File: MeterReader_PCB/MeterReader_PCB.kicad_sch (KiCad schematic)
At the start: 10 parts, among them J1 USB_C_Receptacle_USB2.0, J2 SWD_TagConnect, Q2 AO3401A, SW1 SW_DIP_x04, SW2 SW_Push

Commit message: move active components onto sensor PCB, finish layout of sensor PCB
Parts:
- removed SW1: SW_DIP_x04, symbol Switch:SW_DIP_x04
- added BT2, BT3, BT4: 3.7V LiIon, Battery:BatteryHolder_Keystone_1042_1x18650, symbol Device:Battery_Cell
- added C3: 1u, Capacitor_SMD:C_0603_1608Metric, symbol Device:C
- added C4: 100n, Capacitor_SMD:C_0603_1608Metric, symbol Device:C
- added D1, D2, D3, D4, D5, D6, D7, D8: SS34, Diode_SMD:D_SMA, symbol Device:D_Schottky
- added D10: LED, LED_SMD:LED_0603_1608Metric, symbol Device:LED
- added J6, J7: Conn_01x02, Connector_JST:JST_PH_S2B-PH-K_1x02_P2.00mm_Horizontal, symbol Connector_Generic:Conn_01x02
- added J8: USB_C_Receptacle_USB2.0, Connector_USB:USB_C_Receptacle_HRO_TYPE-C-31-M-12, symbol Connector:USB_C_Receptacle_USB2.0
- added LOGO1: Logo_Open_Hardware_Small, Symbol:OSHW-Symbol_6.7x6mm_SilkScreen, symbol Graphic:Logo_Open_Hardware_Small
- added Q3: FS8205A, Package_SO:TSSOP-8_4.4x3mm_P0.65mm, symbol LeoDJ:FS8205A
- added R10: 1k, Capacitor_SMD:C_0603_1608Metric, symbol Device:R
- added R11, R12, R7: 5k1, Resistor_SMD:R_0603_1608Metric, symbol Device:R
- added R8: 2k2, Resistor_SMD:R_0603_1608Metric, symbol Device:R
- added R9: 100, Capacitor_SMD:C_0603_1608Metric, symbol Device:R
- added TP1, TP2: TestPoint, TestPoint:TestPoint_Pad_1.5x1.5mm, symbol Connector:TestPoint
- added U3: LTC4054ES5-4.2, Package_TO_SOT_SMD:TSOT-23-5, symbol Battery_Management:LTC4054ES5-4.2
- added U4: DW01A, Package_TO_SOT_SMD:SOT-23-6, symbol LeoDJ:DW01A
- BT1: footprint (none) -> Battery:BatteryHolder_Keystone_1042_1x18650
- J2: footprint Connector:Tag-Connect_TC2030-IDC-NL_2x03_P1.27mm_Vertical -> LeoDJ-kicad:Paw-Connect_TC2030-IDC-NL_2x03_P1.27mm_Vertical
- J3: renamed from J?; footprint (none) -> Connector_PinHeader_2.54mm:PinHeader_1x04_P2.54mm_Vertical
- R1, R2, R6: footprint (none) -> Resistor_SMD:R_0603_1608Metric
- SW2: footprint (none) -> Button_Switch_SMD:SW_SPST_TL3342
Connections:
- net +BATT_RAW: now also D1.1 (K), D2.1 (K), D6.1 (K), D8.1 (K), J6.1 (Pin_1), J7.1 (Pin_1), R9.1; no longer BT1.1 (+)
- net GND: now also SW2.2, C3.2, J6.2 (Pin_2), J7.2 (Pin_2), J8.A1 (GND), J8.A12 (GND), J8.B1 (GND), J8.B12 (GND), J8.S1 (SHIELD), Q3.6 (S2), R10.2, R11.2, R12.2, R8.2, U3.2 (GND); no longer BT1.2 (-)
- net VBUS: now also C3.1, J8.A4 (VBUS), J8.A9 (VBUS), J8.B4 (VBUS), J8.B9 (VBUS), U3.4 (VCC)
- net MCU/Button_1: now reaches SW2.1
- net +1V8: now reaches J2.1 (Pin_1)
- net +1V8: now also R7.2
- new net: J8.A5 (CC1), R11.1
- new net: J8.B5 (CC2), R12.1
- new net: BT3.1 (+), D5.1 (K), D6.2 (A)
- new net: Q3.4 (G1), U4.1 (OD)
- new net: Q3.5 (G2), U4.3 (OC)
- new net: BT4.1 (+), D7.1 (K), D8.2 (A)
- new net: BT2.1 (+), D1.2 (A), D3.1 (K)
- new net: R8.1, U3.5 (PROG)
- new net: C4.2, R9.2, U4.5 (VCC)
- new net: BT1.1 (+), D2.2 (A), D4.1 (K)
- new net: D10.2 (A), R7.1
- new net: R10.1, U4.2 (CS)
- new net +BATT_CHG: D3.2 (A), D4.2 (A), D5.2 (A), D7.2 (A), U3.3 (BAT)
- new net -BATT_RAW: BT1.2 (-), BT2.2 (-), BT3.2 (-), BT4.2 (-), C4.1, Q3.2 (S1), U4.6 (GND)
- new net MCU/LED_0: D10.1 (K)
- new net MCU/UART_RX: TP1.1
- new net MCU/UART_TX: TP2.1
- no-connect marks 2 -> 11
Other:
- sheet MCU ports: added Button_1, Button_2, Button_3, LED_0, LED_2, UART_RX, UART_TX; removed Button, LED
- note added: "2k2 = 450mA charging current"
- note added: "Optional bottom placement of additional cells"
- moved on the sheet: BT1, J2, J3, Q2, R6, SW2

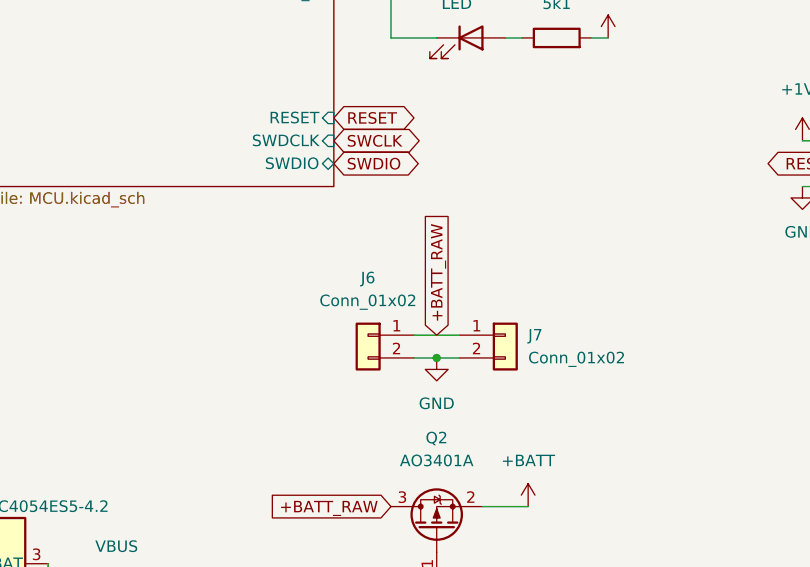
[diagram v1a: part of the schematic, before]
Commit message: add VBUS diode and trace to MCU
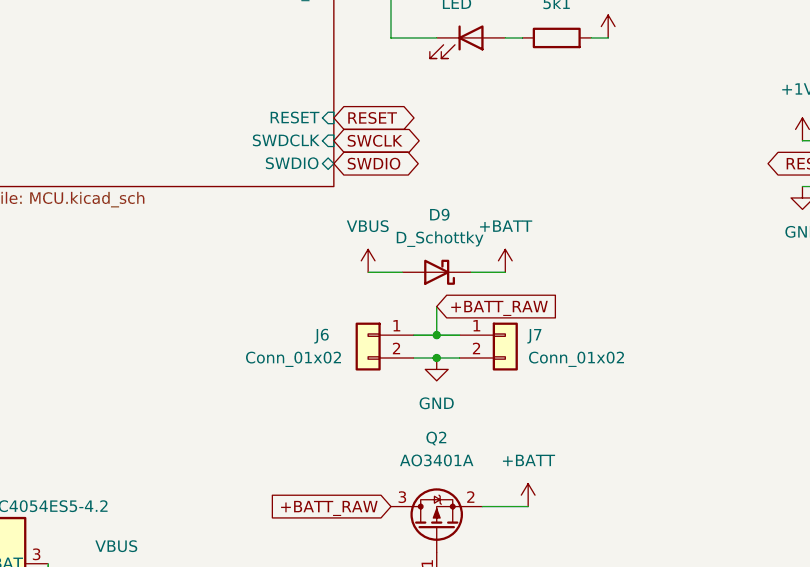
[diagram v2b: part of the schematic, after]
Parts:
- added D9: D_Schottky, Diode_SMD:D_SOD-323, symbol Device:D_Schottky
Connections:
- net +BATT: now also D9.1 (K)
- net VBUS: now also D9.2 (A)
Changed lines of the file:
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@@
   (junction (at 142.24 179.07) (diameter 0) (color 0 0 0 0)
+  )
+  (junction (at 133.35 91.44) (diameter 0) (color 0 0 0 0)
   )
   (junction (at 26.67 121.92) (diameter 0.9144) (color 0 0 0 0)
@@
     (stroke (width 0) (type solid) (color 0 0 0 0))
   )
+  (wire (pts (xy 140.97 84.455) (xy 137.16 84.455))
+    (stroke (width 0) (type default) (color 0 0 0 0))
+  )
   (wire (pts (xy 31.75 134.62) (xy 31.75 146.685))
     (stroke (width 0) (type default) (color 0 0 0 0))
@@
     (stroke (width 0) (type default) (color 0 0 0 0))
   )
+  (wire (pts (xy 133.35 88.265) (xy 133.35 91.44))
+    (stroke (width 0) (type default) (color 0 0 0 0))
+  )
   (wire (pts (xy 41.91 88.9) (xy 44.45 88.9))
     (stroke (width 0) (type solid) (color 0 0 0 0))
@@
     (stroke (width 0) (type solid) (color 0 0 0 0))
   )
-  (wire (pts (xy 130.81 91.44) (xy 135.89 91.44))
+  (wire (pts (xy 133.35 91.44) (xy 135.89 91.44))
+    (stroke (width 0) (type default) (color 0 0 0 0))
+  )
+  (wire (pts (xy 130.81 91.44) (xy 133.35 91.44))
     (stroke (width 0) (type default) (color 0 0 0 0))
   )
@@
   (wire (pts (xy 142.24 179.07) (xy 142.24 182.88))
     (stroke (width 0) (type solid) (color 0 0 0 0))
+  )
+  (wire (pts (xy 125.73 84.455) (xy 129.54 84.455))
+    (stroke (width 0) (type default) (color 0 0 0 0))
   )
   (text "2k2 = 450mA charging current\n" (at 52.07 129.54 0)
@@
     )
   )
-  (global_label "+BATT_RAW" (shape input) (at 133.35 91.44 90) (fields_autoplaced)
+  (global_label "+BATT_RAW" (shape input) (at 133.35 88.265 0) (fields_autoplaced)
     (effects (font (size 1.27 1.27)) (justify left))
-    (property "Intersheet References" "${INTERSHEET_REFS}" (id 0) (at 133.2706 78.3831 90)
+    (property "Intersheet References" "${INTERSHEET_REFS}" (id 0) (at 146.4069 88.1856 0)
       (effects (font (size 1.27 1.27)) (justify left) hide)
     )
@@
     (pin "2")
   )
+  (symbol (lib_id "Device:D_Schottky") (at 133.35 84.455 180) (unit 1)
+    (in_bom yes) (on_board yes) (fields_autoplaced)
+    (property "Reference" "D9" (id 0) (at 133.6675 78.105 0))
+    (property "Value" "D_Schottky" (id 1) (at 133.6675 80.645 0))
+    (property "Footprint" "Diode_SMD:D_SOD-323" (id 2) (at 133.35 84.455 0)
+      (effects (font (size 1.27 1.27)) hide)
+    )
+    (property "Datasheet" "~" (id 3) (at 133.35 84.455 0)
+      (effects (font (size 1.27 1.27)) hide)
+    )
+    (pin "1")
+    (pin "2")
+  )
   (symbol (lib_id "Connector:USB_C_Receptacle_USB2.0") (at 27.94 44.45 0) (unit 1)
     (in_bom yes) (on_board yes)
@@
     (pin "1")
   )
+  (symbol (lib_id "power:VBUS") (at 125.73 84.455 0) (unit 1)
+    (in_bom yes) (on_board yes) (fields_autoplaced)
+    (property "Reference" "#PWR0119" (id 0) (at 125.73 88.265 0)
+      (effects (font (size 1.27 1.27)) hide)
+    )
+    (property "Value" "VBUS" (id 1) (at 125.73 79.375 0))
+    (property "Footprint" "" (id 2) (at 125.73 84.455 0)
+      (effects (font (size 1.27 1.27)) hide)
+    )
+    (property "Datasheet" "" (id 3) (at 125.73 84.455 0)
+      (effects (font (size 1.27 1.27)) hide)
+    )
+    (pin "1")
+  )
   (symbol (lib_id "Device:D_Schottky") (at 21.59 150.495 270) (unit 1)
     (in_bom yes) (on_board yes)
@@
     (pin "4")
   )
+  (symbol (lib_id "power:+BATT") (at 140.97 84.455 0) (unit 1)
+    (in_bom yes) (on_board yes) (fields_autoplaced)
+    (property "Reference" "#PWR0118" (id 0) (at 140.97 88.265 0)
+      (effects (font (size 1.27 1.27)) hide)
+    )
+    (property "Value" "+BATT" (id 1) (at 140.97 79.375 0))
+    (property "Footprint" "" (id 2) (at 140.97 84.455 0)
+      (effects (font (size 1.27 1.27)) hide)
+    )
+    (property "Datasheet" "" (id 3) (at 140.97 84.455 0)
+      (effects (font (size 1.27 1.27)) hide)
+    )
+    (pin "1")
+  )
   (symbol (lib_id "Connector_Generic:Conn_02x03_Odd_Even") (at 184.15 72.39 0) (unit 1)
     (in_bom yes) (on_board yes) (fields_autoplaced)
@@
   )
   (symbol (lib_id "Connector_Generic:Conn_01x02") (at 125.73 91.44 0) (mirror y) (unit 1)
-    (in_bom yes) (on_board yes) (fields_autoplaced)
-    (property "Reference" "J6" (id 0) (at 125.73 85.09 0))
-    (property "Value" "Conn_01x02" (id 1) (at 125.73 87.63 0))
+    (in_bom yes) (on_board yes)
+    (property "Reference" "J6" (id 0) (at 120.65 91.44 0))
+    (property "Value" "Conn_01x02" (id 1) (at 117.475 93.98 0))
     (property "Footprint" "Connector_JST:JST_PH_S2B-PH-K_1x02_P2.00mm_Horizontal" (id 2) (at 125.73 91.44 0)
       (effects (font (size 1.27 1.27)) hide)
@@
       (reference "#PWR0117") (unit 1) (value "GND") (footprint "")
     )
+    (path "/9badaafb-6255-4ef3-89e0-7dc40e33ba7c"
+      (reference "#PWR0118") (unit 1) (value "+BATT") (footprint "")
+    )
+    (path "/790bc80a-1db8-4da0-938c-b4944cd5b566"
+      (reference "#PWR0119") (unit 1) (value "VBUS") (footprint "")
+    )
     (path "/44dca144-98db-4bce-8f23-174888978dbb"
       (reference "#PWR0120") (unit 1) (value "+1V8") (footprint "")
@@
       (reference "D8") (unit 1) (value "SS34") (footprint "Diode_SMD:D_SMA")
     )
+    (path "/655956d5-86e7-47e4-bb1a-09ebb0ca06bb"
+      (reference "D9") (unit 1) (value "D_Schottky") (footprint "Diode_SMD:D_SOD-323")
+    )
     (path "/7171410f-4042-4ba3-bc0f-c57ed24c61a6"

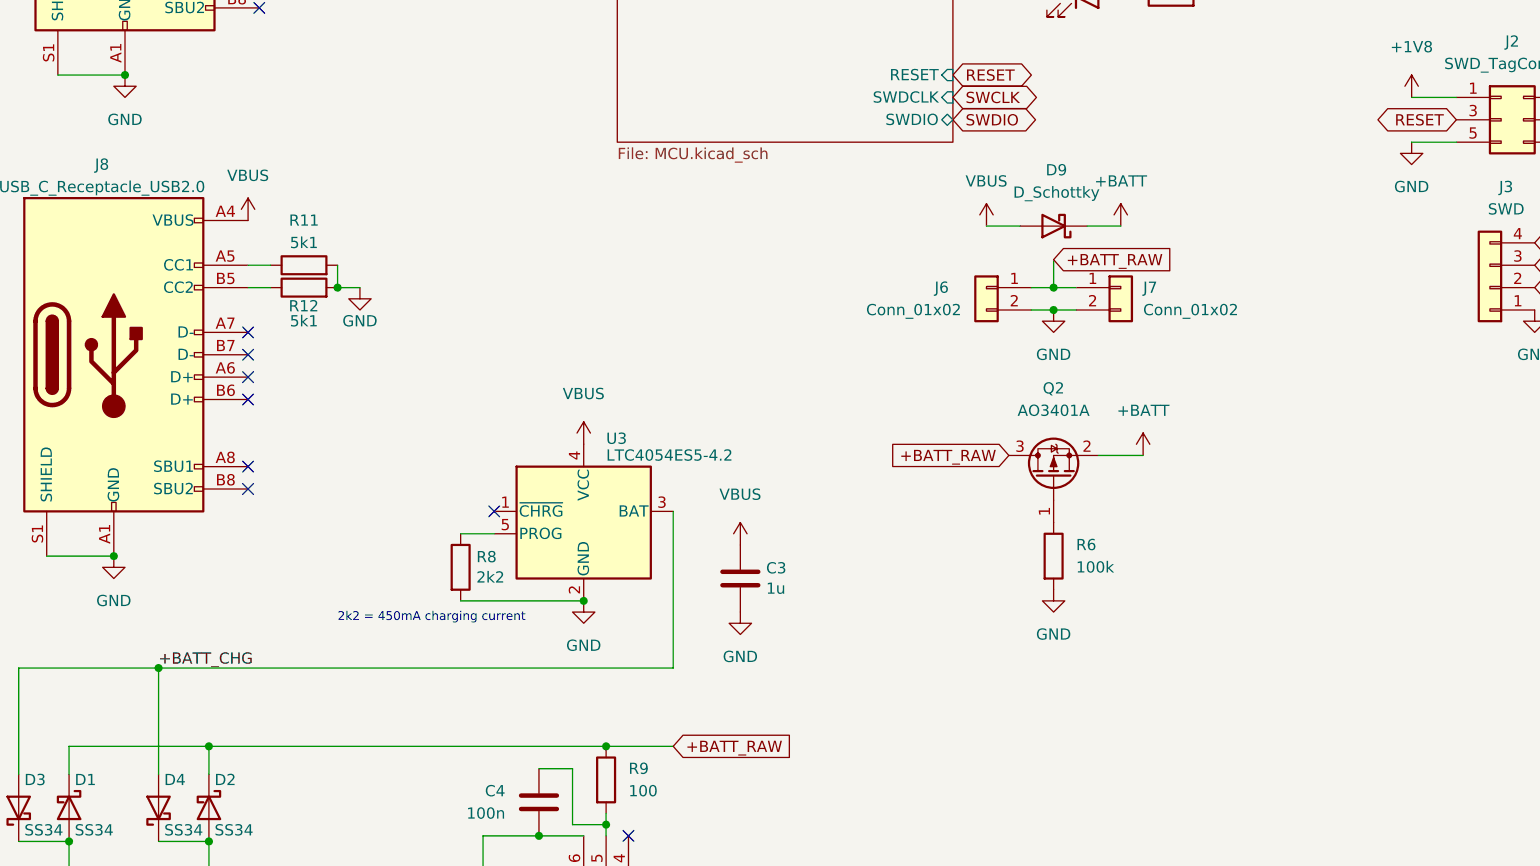
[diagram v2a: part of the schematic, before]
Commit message: finish layout of battery pack PCB
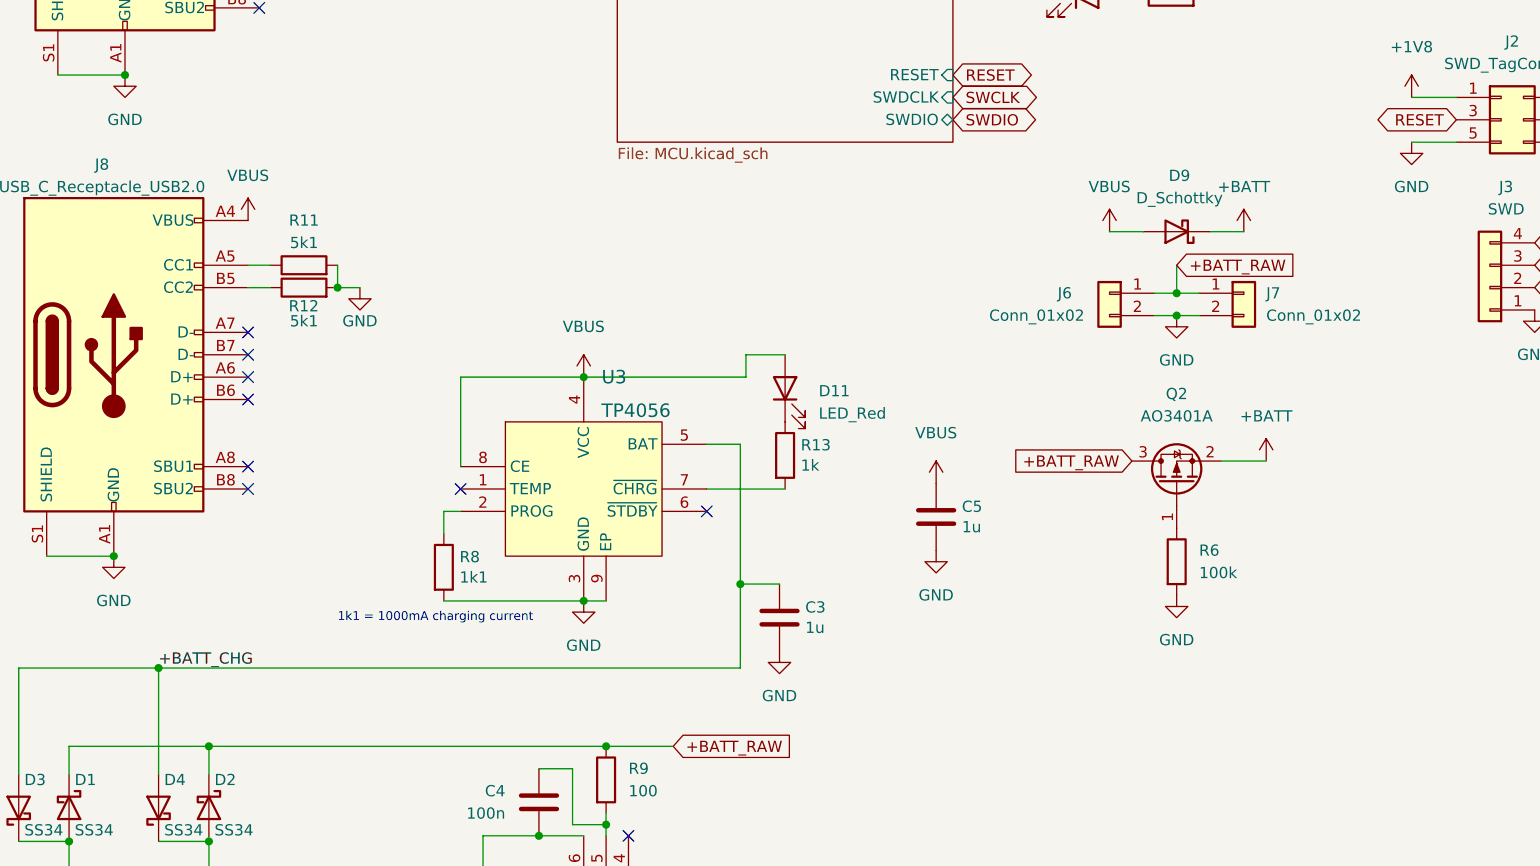
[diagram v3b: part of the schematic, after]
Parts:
- removed U3: LTC4054ES5-4.2, Package_TO_SOT_SMD:TSOT-23-5, symbol Battery_Management:LTC4054ES5-4.2
- added C5: 1u, Capacitor_SMD:C_0603_1608Metric, symbol Device:C
- added D11: LED_Red, LED_SMD:LED_0603_1608Metric, symbol Device:LED
- added R13: 1k, Resistor_SMD:R_0603_1608Metric, symbol Device:R
- added U3: TP4056, Package_SO:SOIC-8-1EP_3.9x4.9mm_P1.27mm_EP2.41x3.3mm_ThermalVias, symbol LeoDJ:TP4056
- R8: value 2k2 -> 1k1
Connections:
- net +BATT_CHG: now also C3.1, U3.5 (BAT)
- net GND: now also C5.2, U3.3 (GND), U3.9 (EP)
- net VBUS: now also C5.1, D11.2 (A), U3.4 (VCC), U3.8 (CE); no longer C3.1
- net at R8.1: now also U3.2 (PROG)
- new net: D11.1 (K), R13.1
- new net: R13.2, U3.7 (~{CHRG})
- no-connect marks 11 -> 12
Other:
- note added: "1k1 = 1000mA charging current"
- note removed: "2k2 = 450mA charging current"
- moved on the sheet: C3, D9, J6, J7, Q2, R6, R8
